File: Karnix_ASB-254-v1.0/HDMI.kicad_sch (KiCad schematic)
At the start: 22 parts, among them J19 HDMI_A_1.4

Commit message: Rework HDMI wiring: - Connect SDL, SCL and CEC signals to FPGA through level converters - Separate HDMI power rails with diodes
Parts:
- removed R94: 1.5K/1%, Fabmicro:R_0402_1005Metric, symbol Fabmicro:Resistor
- removed R94: DNM, Fabmicro:R_0402_1005Metric, symbol Fabmicro:Resistor
- removed R94: 27K/1%, Fabmicro:R_0402_1005Metric, symbol Fabmicro:Resistor
- added C122 (x2): 0.1uF/50V, Fabmicro:C_0402_1005Metric, symbol Fabmicro:CapacitorUnpolarized
- added C48 (x2): 10uF/10V, Capacitor_SMD:C_0603_1608Metric, symbol Fabmicro:CapacitorUnpolarized
- added C8: 1uF/16V, Fabmicro:C_0402_1005Metric, symbol Fabmicro:CapacitorUnpolarized
- added D6 (x2): CRS08, Fabmicro:D_SOD-123F, symbol Fabmicro:Diode
- added R101: 22R/1%, Resistor_SMD:R_0402_1005Metric, symbol Fabmicro:Resistor
- added R42: 110R/1%, Fabmicro:R_0402_1005Metric, symbol Fabmicro:Resistor
- added R94 (x4): 5.1K/1%, Fabmicro:R_0402_1005Metric, symbol Fabmicro:Resistor
- added R94 (x4): 1.5K/1%, Fabmicro:R_0402_1005Metric, symbol Fabmicro:Resistor
- added R94: 10K/1%, Fabmicro:R_0402_1005Metric, symbol Fabmicro:Resistor
- added R94: 27K/1%, Fabmicro:R_0402_1005Metric, symbol Fabmicro:Resistor
- added VT3 (x3): DMN3730, Fabmicro:SOT-23, symbol Fabmicro:MOSFET_N_CH_SOT23
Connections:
- net +3V3: now also R94.1, D6.2 (A), R94.1, R94.1, R94.1, R94.1, R94.1, R94.1, R94.1; no longer R97.1, R97.1, R97.1, R97.1, R97.1, R97.1, R97.1, R97.1
- net +5V: now also D6.2 (A); no longer F3.2, R94.1
- net GND: now also C122.2, C122.2, C48.2, C48.2, C8.2, R94.1
- net HDDC_CEC: now reaches J19.13 (CEC)
- net HDDC_CEC: now also R94.2, VT3.3 (D)
- net HDDC_SCL: now reaches J19.15 (SCL)
- net HDDC_SCL: now also R94.2, VT3.3 (D)
- net at R94.2: now also VT3.1 (G); no longer J19.16 (SDA)
- net at J19.18 (+5V): now also F3.2; no longer F3.1
- net at J19.19 (HPD/HEAC-): now also R94.2
- new net: C8.1, R101.2, R94.1, R94.2
- new net: R42.1, R94.2, VT3.2 (S)
- new net: R94.2, VT3.1 (G) (x2)
- new net +3V3_HDMI: C122.1, C48.1, D6.1 (K), R97.1, R97.1, R97.1, R97.1, R97.1, R97.1, R97.1, R97.1
- new net +5V_HDMI: C122.1, C48.1, D6.1 (K), F3.1, R94.1
- new net HDDC_SDA: J19.16 (SDA), R94.2, VT3.3 (D)
- new net HDMI_CEC: R42.2
- new net HDMI_HPD: R101.1
- new net HDMI_SCL: R94.2, VT3.2 (S)
- new net HDMI_SDA: R94.2, VT3.2 (S)
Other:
- moved on the sheet: F3, R94

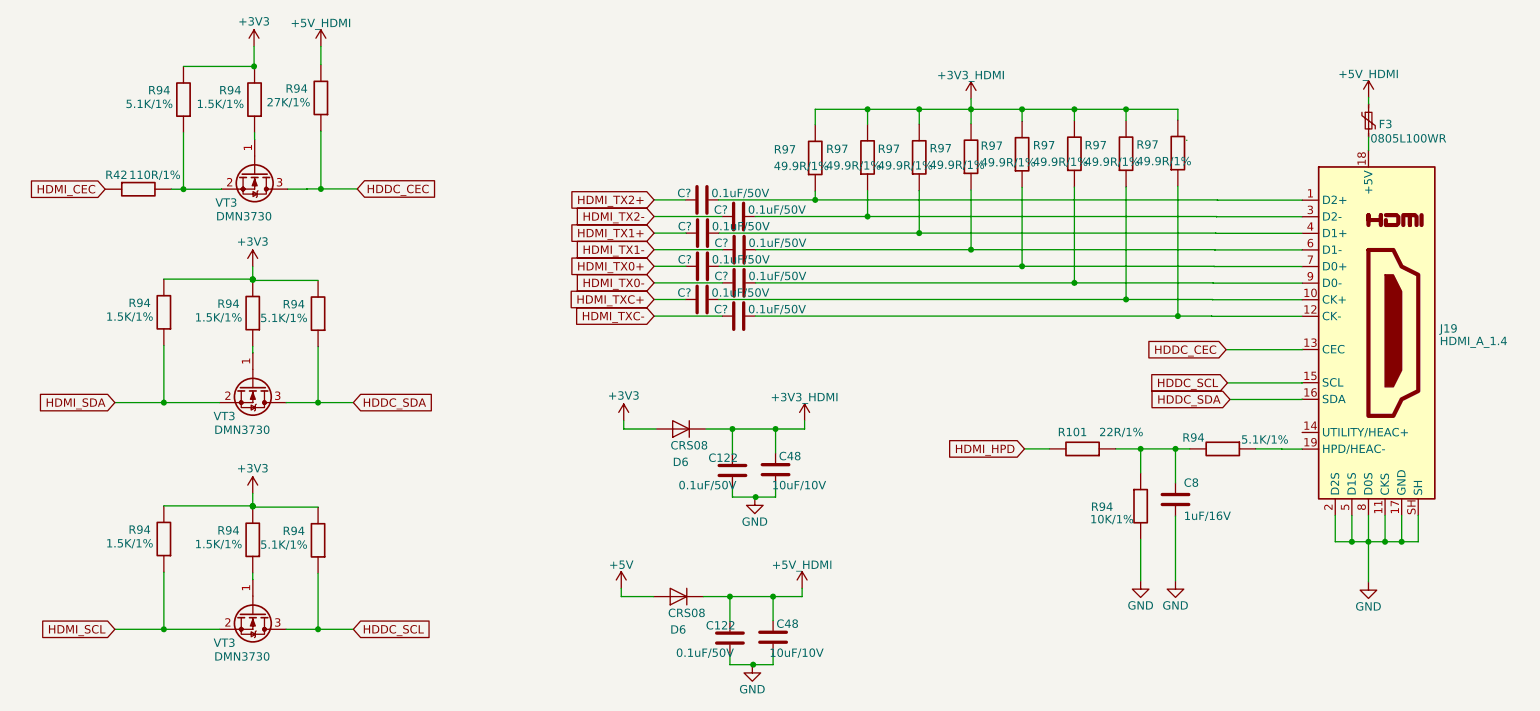
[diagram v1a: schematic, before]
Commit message: Remove rudimentary referencies to old projects
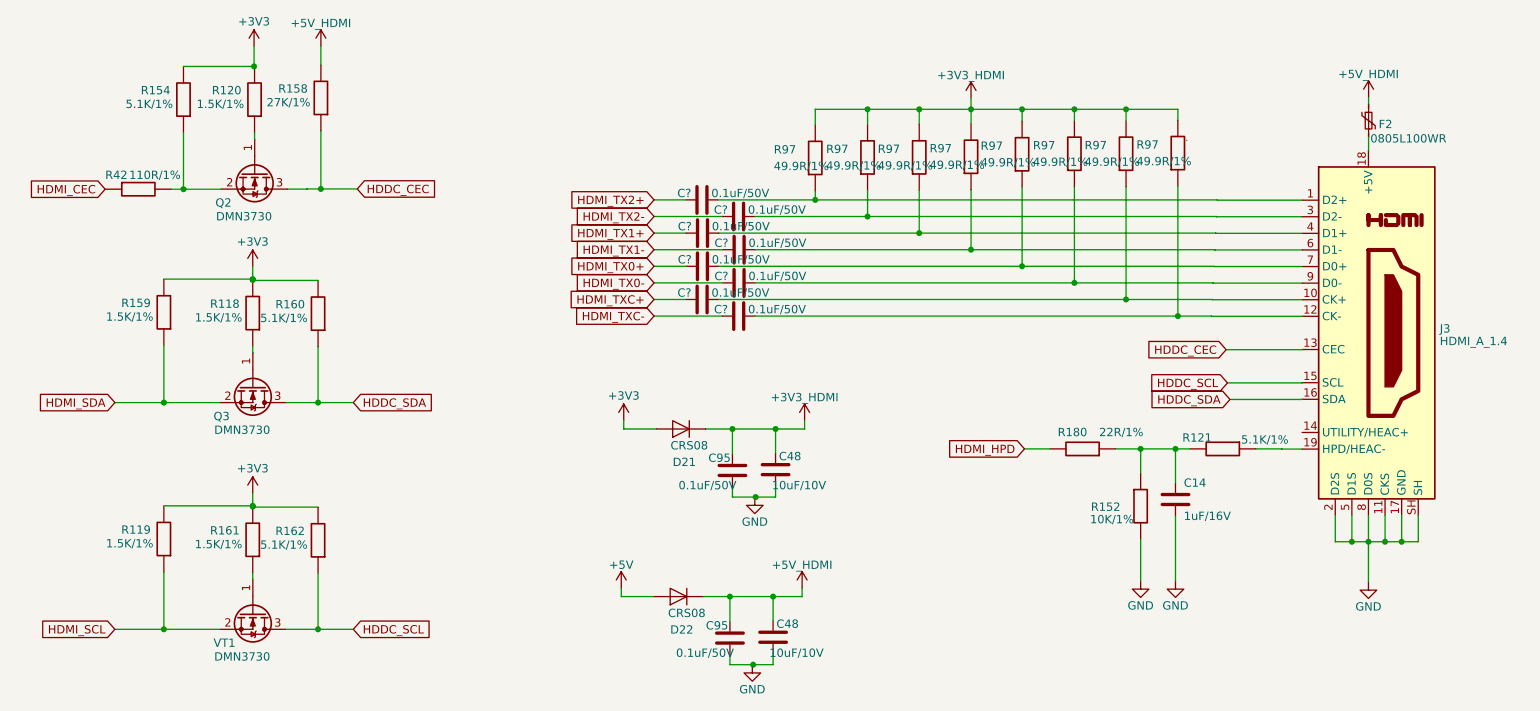
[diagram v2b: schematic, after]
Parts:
- renumbered C8 to C14, C122 to C95, D6 to D21, D6 to D22, F3 to F2, J19 to J3, VT3 to Q2, VT3 to Q3, R94 to R118, R94 to R119, R94 to R120, R94 to R121, R94 to R152, R94 to R154, R94 to R158, R94 to R159, R94 to R160, R94 to R161, R94 to R162, R101 to R180, VT3 to VT1

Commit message: Fix transistor reference: VT1 -> Q4
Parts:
- renumbered VT1 to Q4
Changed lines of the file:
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@@
   (symbol (lib_id "Fabmicro:MOSFET_N_CH_SOT23") (at 75.82 152.58 270) (unit 1)
     (in_bom yes) (on_board yes) (dnp no)
-    (property "Reference" "VT1" (at 69.8 162.3 90)
+    (property "Reference" "Q4" (at 69.8 162.3 90)
       (effects (font (size 1.27 1.27)) (justify left))
     )
@@
       (project "Karnix_ASB"
         (path "/fe37e245-9527-4c72-91fc-09b617a42f73/25c0df33-00ba-4d9b-b094-bedba27f35c8"
-          (reference "VT1") (unit 1)
+          (reference "Q4") (unit 1)
         )
       )
